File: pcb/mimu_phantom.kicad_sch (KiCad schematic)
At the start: 20 parts, among them U3 MCP16331CH

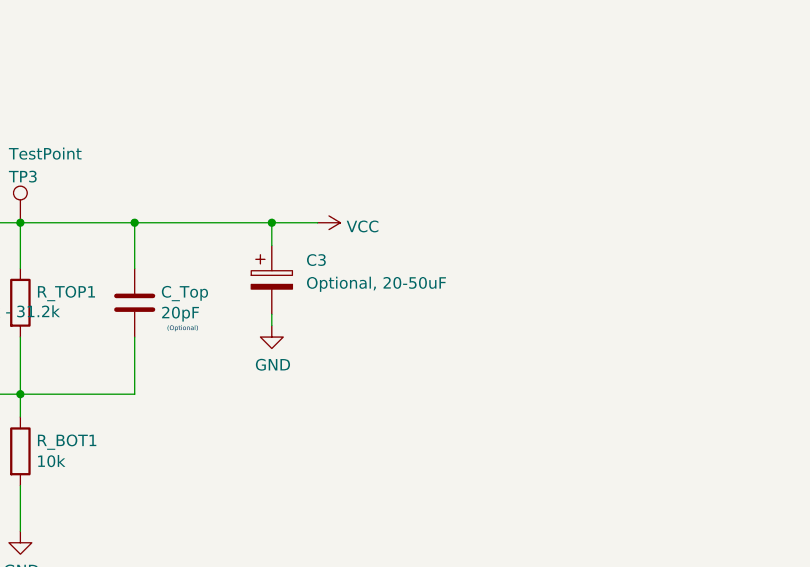
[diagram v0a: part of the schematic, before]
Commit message: Wait for user input on button-press on startup
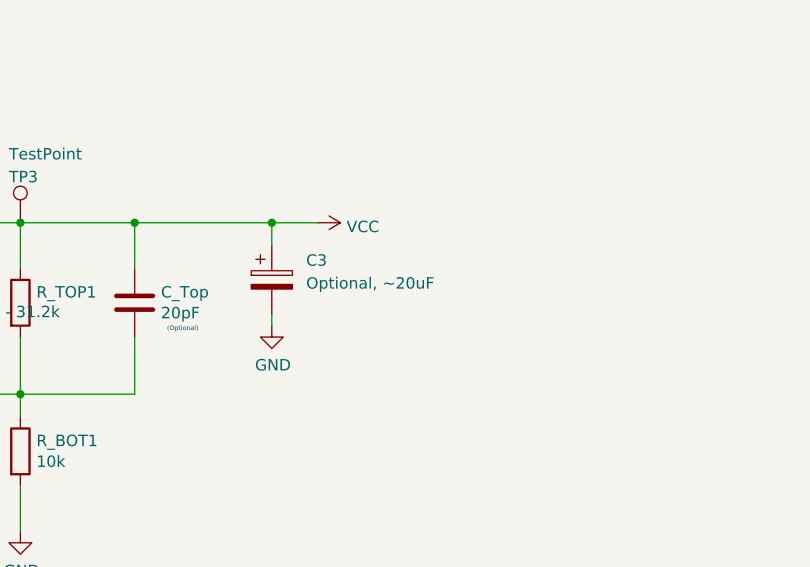
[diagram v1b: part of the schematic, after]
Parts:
- C3: value Optional, 20-50uF -> Optional, ~20uF
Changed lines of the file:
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@@
 			)
 		)
-		(property "Value" "Optional, 20-50uF"
+		(property "Value" "Optional, ~20uF"
 			(at 166.37 135.0009 0)
 			(effects
